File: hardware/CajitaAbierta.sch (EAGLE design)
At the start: 30 parts

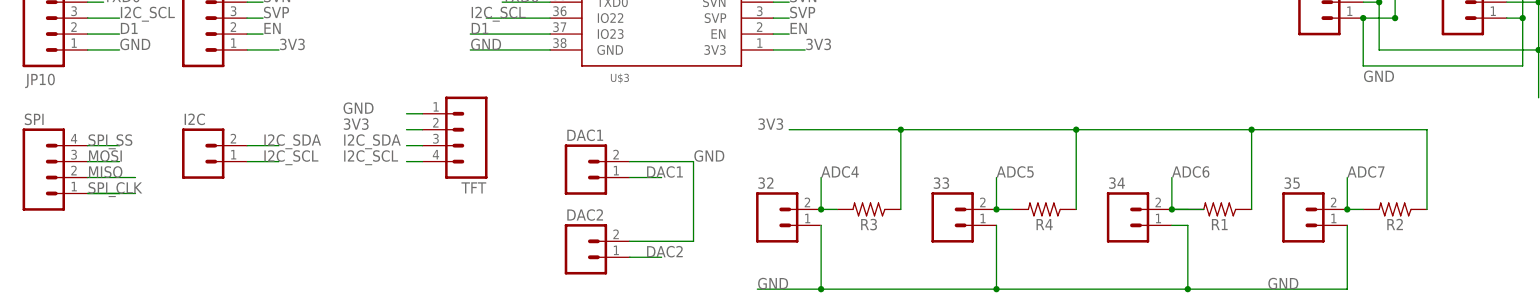
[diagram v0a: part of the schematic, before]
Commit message: Voltage divider uses V+ as variable resistance
For Yesi :)
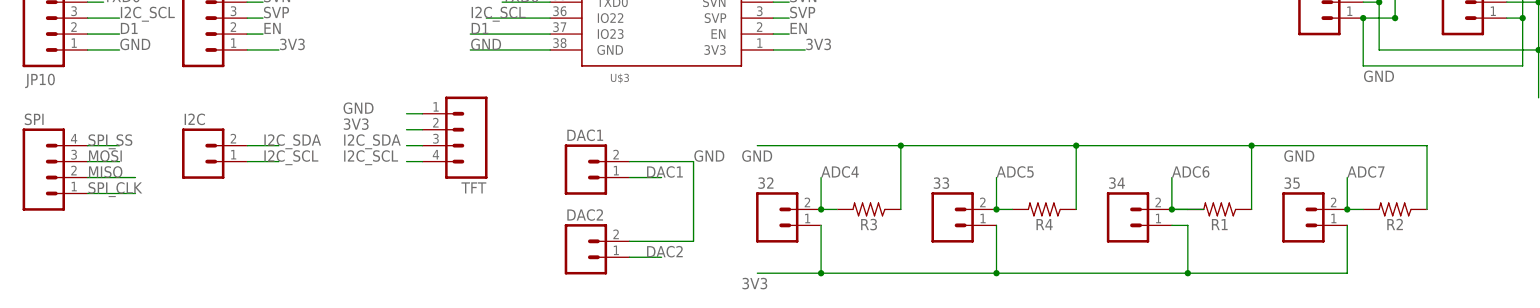
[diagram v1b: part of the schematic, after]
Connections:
- net 3V3: now also 32.1, 33.1, 34.1, 35.1; no longer R1.1, R2.1, R3.1, R4.1
- net GND: now also R1.1, R2.1, R3.1, R4.1; no longer 32.1, 33.1, 34.1, 35.1
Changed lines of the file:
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@@
 </segment>
 <segment>
-<pinref part="35" gate="G$1" pin="1"/>
-<label x="139.7" y="15.24" size="1.778" layer="95"/>
-<wire x1="139.7" y1="15.24" x2="149.86" y2="15.24" width="0.1524" layer="91"/>
-<wire x1="149.86" y1="15.24" x2="177.8" y2="15.24" width="0.1524" layer="91"/>
-<wire x1="177.8" y1="15.24" x2="208.28" y2="15.24" width="0.1524" layer="91"/>
-<wire x1="208.28" y1="15.24" x2="233.68" y2="15.24" width="0.1524" layer="91"/>
-<wire x1="233.68" y1="15.24" x2="233.68" y2="25.4" width="0.1524" layer="91"/>
-<pinref part="32" gate="G$1" pin="1"/>
-<wire x1="149.86" y1="25.4" x2="149.86" y2="15.24" width="0.1524" layer="91"/>
-<junction x="149.86" y="15.24"/>
-<pinref part="33" gate="G$1" pin="1"/>
-<wire x1="177.8" y1="25.4" x2="177.8" y2="15.24" width="0.1524" layer="91"/>
-<junction x="177.8" y="15.24"/>
-<pinref part="34" gate="G$1" pin="1"/>
-<wire x1="205.74" y1="25.4" x2="208.28" y2="25.4" width="0.1524" layer="91"/>
-<label x="220.98" y="15.24" size="1.778" layer="95"/>
-<wire x1="208.28" y1="25.4" x2="208.28" y2="15.24" width="0.1524" layer="91"/>
-<junction x="208.28" y="15.24"/>
+<label x="137.16" y="35.56" size="1.778" layer="95"/>
+<wire x1="139.7" y1="38.1" x2="162.56" y2="38.1" width="0.1524" layer="91"/>
+<label x="223.52" y="35.56" size="1.778" layer="95"/>
+<pinref part="R2" gate="G$1" pin="1"/>
+<wire x1="162.56" y1="38.1" x2="190.5" y2="38.1" width="0.1524" layer="91"/>
+<wire x1="190.5" y1="38.1" x2="218.44" y2="38.1" width="0.1524" layer="91"/>
+<wire x1="218.44" y1="38.1" x2="246.38" y2="38.1" width="0.1524" layer="91"/>
+<wire x1="246.38" y1="27.94" x2="246.38" y2="38.1" width="0.1524" layer="91"/>
+<pinref part="R1" gate="G$1" pin="1"/>
+<wire x1="218.44" y1="27.94" x2="218.44" y2="38.1" width="0.1524" layer="91"/>
+<junction x="218.44" y="38.1"/>
+<pinref part="R4" gate="G$1" pin="1"/>
+<wire x1="190.5" y1="27.94" x2="190.5" y2="38.1" width="0.1524" layer="91"/>
+<junction x="190.5" y="38.1"/>
+<pinref part="R3" gate="G$1" pin="1"/>
+<wire x1="162.56" y1="27.94" x2="162.56" y2="38.1" width="0.1524" layer="91"/>
+<junction x="162.56" y="38.1"/>
 </segment>
 <segment>
@@
 <segment>
 <wire x1="40.64" y1="30.48" x2="33.02" y2="30.48" width="0.1524" layer="91"/>
-<wire x1="33.02" y1="30.48" x2="38.1" y2="30.48" width="0.1524" layer="91"/>
 <pinref part="SPI" gate="G$1" pin="1"/>
 <label x="33.02" y="30.48" size="1.778" layer="95"/>
@@
 </segment>
 <segment>
-<pinref part="R1" gate="G$1" pin="1"/>
-<wire x1="144.78" y1="40.64" x2="162.56" y2="40.64" width="0.1524" layer="91"/>
-<wire x1="162.56" y1="40.64" x2="190.5" y2="40.64" width="0.1524" layer="91"/>
-<label x="139.7" y="40.64" size="1.778" layer="95"/>
-<pinref part="R3" gate="G$1" pin="1"/>
-<wire x1="162.56" y1="27.94" x2="162.56" y2="40.64" width="0.1524" layer="91"/>
-<junction x="162.56" y="40.64"/>
-<pinref part="R4" gate="G$1" pin="1"/>
-<wire x1="190.5" y1="27.94" x2="190.5" y2="40.64" width="0.1524" layer="91"/>
-<junction x="190.5" y="40.64"/>
-<pinref part="R2" gate="G$1" pin="1"/>
-<wire x1="190.5" y1="40.64" x2="218.44" y2="40.64" width="0.1524" layer="91"/>
-<wire x1="218.44" y1="40.64" x2="246.38" y2="40.64" width="0.1524" layer="91"/>
-<wire x1="246.38" y1="40.64" x2="246.38" y2="27.94" width="0.1524" layer="91"/>
-<wire x1="218.44" y1="27.94" x2="218.44" y2="40.64" width="0.1524" layer="91"/>
-<junction x="218.44" y="40.64"/>
-</segment>
-</net>
+<label x="137.16" y="15.24" size="1.778" layer="95"/>
+<wire x1="139.7" y1="17.78" x2="149.86" y2="17.78" width="0.1524" layer="91"/>
+<pinref part="32" gate="G$1" pin="1"/>
+<wire x1="149.86" y1="17.78" x2="177.8" y2="17.78" width="0.1524" layer="91"/>
+<wire x1="177.8" y1="17.78" x2="208.28" y2="17.78" width="0.1524" layer="91"/>
+<wire x1="208.28" y1="17.78" x2="233.68" y2="17.78" width="0.1524" layer="91"/>
+<wire x1="149.86" y1="25.4" x2="149.86" y2="17.78" width="0.1524" layer="91"/>
+<junction x="149.86" y="17.78"/>
+<pinref part="33" gate="G$1" pin="1"/>
+<wire x1="177.8" y1="25.4" x2="177.8" y2="17.78" width="0.1524" layer="91"/>
+<junction x="177.8" y="17.78"/>
+<pinref part="34" gate="G$1" pin="1"/>
+<wire x1="205.74" y1="25.4" x2="208.28" y2="25.4" width="0.1524" layer="91"/>
+<wire x1="208.28" y1="25.4" x2="208.28" y2="17.78" width="0.1524" layer="91"/>
+<junction x="208.28" y="17.78"/>
+<pinref part="35" gate="G$1" pin="1"/>
+<wire x1="233.68" y1="25.4" x2="233.68" y2="17.78" width="0.1524" layer="91"/>
+</segment>
+</net>

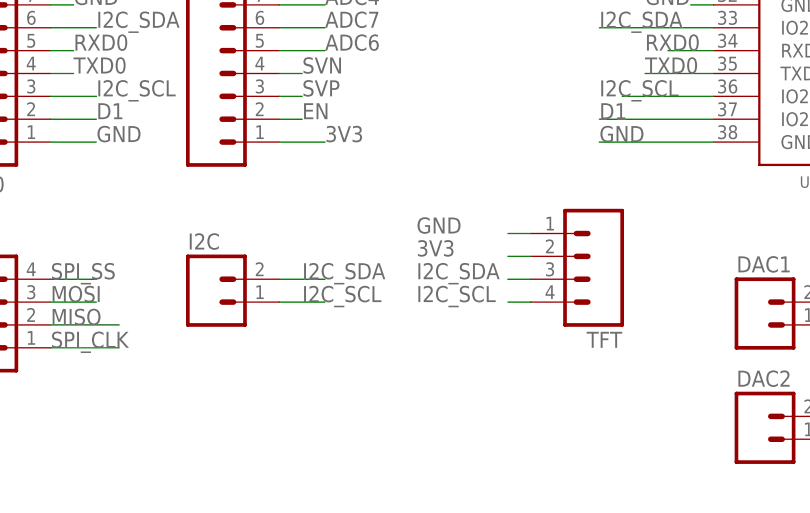
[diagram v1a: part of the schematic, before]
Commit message: v04 - changes to the TFT connections
nouvelles étiquettes (labels)
cambié sdl and sda
switch on the other side
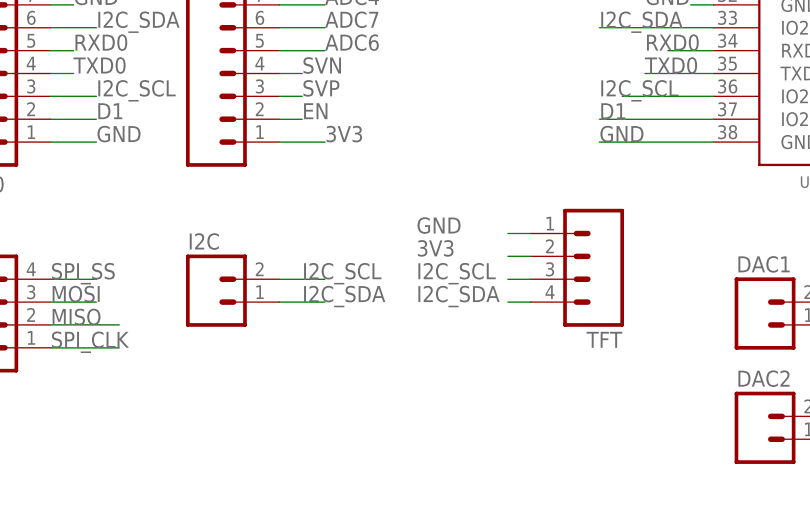
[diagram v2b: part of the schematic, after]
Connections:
- net I2C_SCL: now also I2C.2, TFT.3; no longer I2C.1, TFT.4
- net I2C_SDA: now also I2C.1, TFT.4; no longer I2C.2, TFT.3
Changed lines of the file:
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@@
 </segment>
 </net>
-<net name="I2C_SDA" class="0">
-<segment>
-<pinref part="U$3" gate="G$1" pin="IO21"/>
-<wire x1="106.68" y1="66.04" x2="93.98" y2="66.04" width="0.1524" layer="91"/>
-<label x="93.98" y="66.04" size="1.778" layer="95"/>
-</segment>
-<segment>
-<pinref part="JP10" gate="G$1" pin="6"/>
-<label x="38.1" y="66.04" size="1.778" layer="95"/>
-<wire x1="33.02" y1="66.04" x2="38.1" y2="66.04" width="0.1524" layer="91"/>
+<net name="I2C_SCL" class="0">
+<segment>
+<pinref part="JP10" gate="G$1" pin="3"/>
+<label x="38.1" y="58.42" size="1.778" layer="95"/>
+<wire x1="33.02" y1="58.42" x2="38.1" y2="58.42" width="0.1524" layer="91"/>
+</segment>
+<segment>
+<pinref part="U$3" gate="G$1" pin="IO22"/>
+<wire x1="106.68" y1="58.42" x2="96.52" y2="58.42" width="0.1524" layer="91"/>
+<label x="93.98" y="58.42" size="1.778" layer="95"/>
 </segment>
 <segment>
@@
 <wire x1="58.42" y1="38.1" x2="63.5" y2="38.1" width="0.1524" layer="91"/>
 <label x="60.96" y="38.1" size="1.778" layer="95"/>
-</segment>
-</net>
-<net name="I2C_SCL" class="0">
-<segment>
-<pinref part="TFT" gate="G$1" pin="4"/>
-<wire x1="83.82" y1="35.56" x2="86.36" y2="35.56" width="0.1524" layer="91"/>
-<label x="73.66" y="35.56" size="1.778" layer="95"/>
-</segment>
-<segment>
-<pinref part="JP10" gate="G$1" pin="3"/>
-<label x="38.1" y="58.42" size="1.778" layer="95"/>
-<wire x1="33.02" y1="58.42" x2="38.1" y2="58.42" width="0.1524" layer="91"/>
-</segment>
-<segment>
-<pinref part="U$3" gate="G$1" pin="IO22"/>
-<wire x1="106.68" y1="58.42" x2="96.52" y2="58.42" width="0.1524" layer="91"/>
-<label x="93.98" y="58.42" size="1.778" layer="95"/>
-</segment>
-<segment>
-<pinref part="I2C" gate="G$1" pin="1"/>
-<wire x1="63.5" y1="35.56" x2="58.42" y2="35.56" width="0.1524" layer="91"/>
-<label x="60.96" y="35.56" size="1.778" layer="95"/>
 </segment>
 </net>
@@
 </segment>
 </net>
+<net name="I2C_SDA" class="0">
+<segment>
+<pinref part="TFT" gate="G$1" pin="4"/>
+<wire x1="86.36" y1="35.56" x2="83.82" y2="35.56" width="0.1524" layer="91"/>
+<label x="73.66" y="35.56" size="1.778" layer="95"/>
+</segment>
+<segment>
+<pinref part="I2C" gate="G$1" pin="1"/>
+<wire x1="58.42" y1="35.56" x2="63.5" y2="35.56" width="0.1524" layer="91"/>
+<label x="60.96" y="35.56" size="1.778" layer="95"/>
+</segment>
+<segment>
+<pinref part="JP10" gate="G$1" pin="6"/>
+<label x="38.1" y="66.04" size="1.778" layer="95"/>
+<wire x1="33.02" y1="66.04" x2="38.1" y2="66.04" width="0.1524" layer="91"/>
+</segment>
+<segment>
+<pinref part="U$3" gate="G$1" pin="IO21"/>
+<wire x1="106.68" y1="66.04" x2="93.98" y2="66.04" width="0.1524" layer="91"/>
+<label x="93.98" y="66.04" size="1.778" layer="95"/>
+</segment>
+</net>

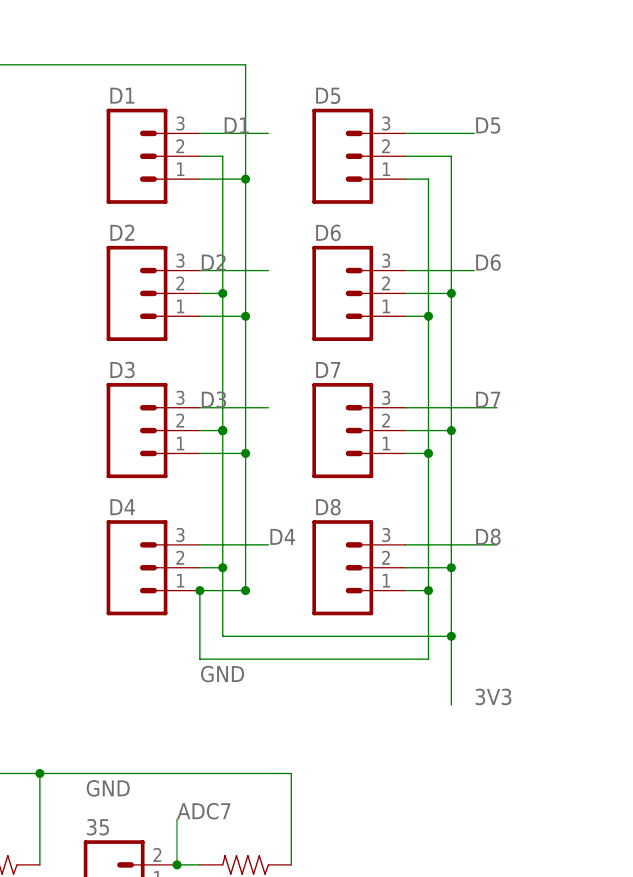
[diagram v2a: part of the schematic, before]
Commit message: Now with screw terminals
More code examples
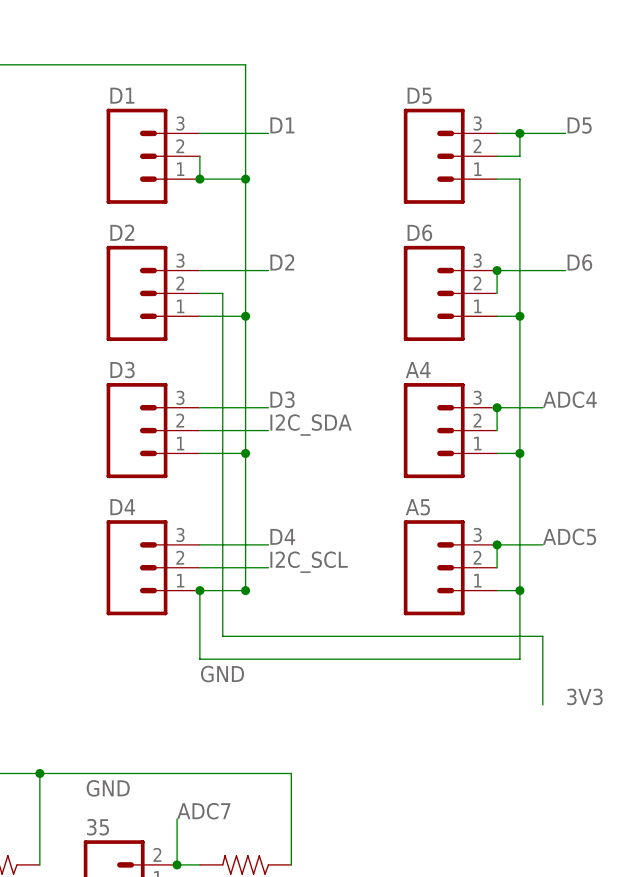
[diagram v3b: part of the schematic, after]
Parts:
- removed D7, D8: (no value), SparkFun-Connectors:M03LOCK_LONGPADS
- added A4, A5: (no value), SparkFun-Connectors:M03LOCK_LONGPADS
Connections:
- net 3V3: no longer D1.2, D3.2, D4.2, D5.2, D6.2, D7.2, D8.2
- net ADC4: now also A4.2, A4.3
- net ADC5: now also A5.2, A5.3
- net D5: now also D5.2
- net D6: now also D6.2
- net D7: no longer D7.3
- net D8: no longer D8.3
- net GND: now also A4.1, A5.1, D1.2; no longer D7.1, D8.1
- net I2C_SCL: now also D4.2
- net I2C_SDA: now also D3.2
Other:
- moved on the sheet: D5, D6
